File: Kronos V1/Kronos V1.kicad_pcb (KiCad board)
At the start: 4 copper layers, 65.6 x 91.8 mm, 229 parts, among them IC1 AS5600-ASOT, J1 USB_C_Receptacle_USB2.0_16P, Q1 BSS138, Q2 BSS138, U1 DM-OLED096-636, U10 ADS1115IDGS, U11 ADS1115IDGS, U12 WS2812-2020, U13 WS2812-2020, U14 WS2812-2020, U15 WS2812-2020, U16 WS2812-2020, U17 WS2812-2020, U18 WS2812-2020, U19 WS2812-2020, U2 ESP32-S3-MINI-1, U20 WS2812-2020, U21 WS2812-2020, U22 WS2812-2020, U23 WS2812-2020, U24 WS2812-2020, U25 WS2812-2020, U26 WS2812-2020, U27 WS2812-2020, U28 WS2812-2020, U29 WS2812-2020, U3 AMS1117-3.3, U30 WS2812-2020, U31 WS2812-2020, U32 WS2812-2020, U33 WS2812-2020, U34 WS2812-2020, U35 WS2812-2020, U36 WS2812-2020, U37 WS2812-2020, U38 WS2812-2020, U39 WS2812-2020, U4 AH49ENTR-G1, U40 WS2812-2020, U41 WS2812-2020, U42 WS2812-2020, U43 WS2812-2020, U44 WS2812-2020, U45 WS2812-2020, U46 WS2812-2020, U47 WS2812-2020, U48 WS2812-2020, U49 WS2812-2020, U5 AH49ENTR-G1, U50 WS2812-2020, U51 WS2812-2020, U52 WS2812-2020, U53 WS2812-2020, U54 WS2812-2020, U55 WS2812-2020, U56 WS2812-2020, U57 WS2812-2020, U58 WS2812-2020, U59 WS2812-2020, U6 AH49ENTR-G1, U60 WS2812-2020, U61 WS2812-2020, U62 WS2812-2020, U63 WS2812-2020, U64 WS2812-2020, U65 WS2812-2020, U66 WS2812-2020, U67 WS2812-2020, U68 WS2812-2020, U69 WS2812-2020, U7 AH49ENTR-G1, U70 WS2812-2020, U71 WS2812-2020, U72 WS2812-2020, U73 WS2812-2020, U74 WS2812-2020, U75 WS2812-2020, U76 WS2812-2020, U77 WS2812-2020, U78 WS2812-2020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

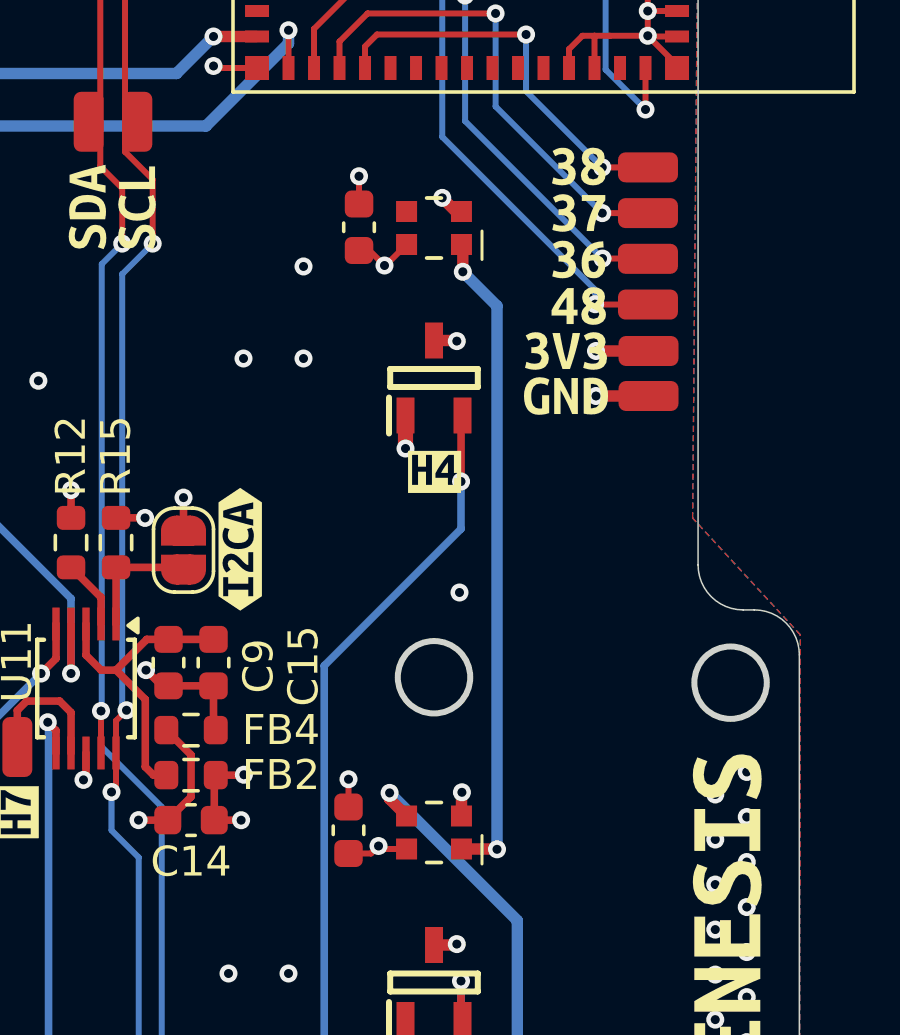
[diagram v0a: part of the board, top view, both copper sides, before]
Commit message: Corrected error with H4 ARGB
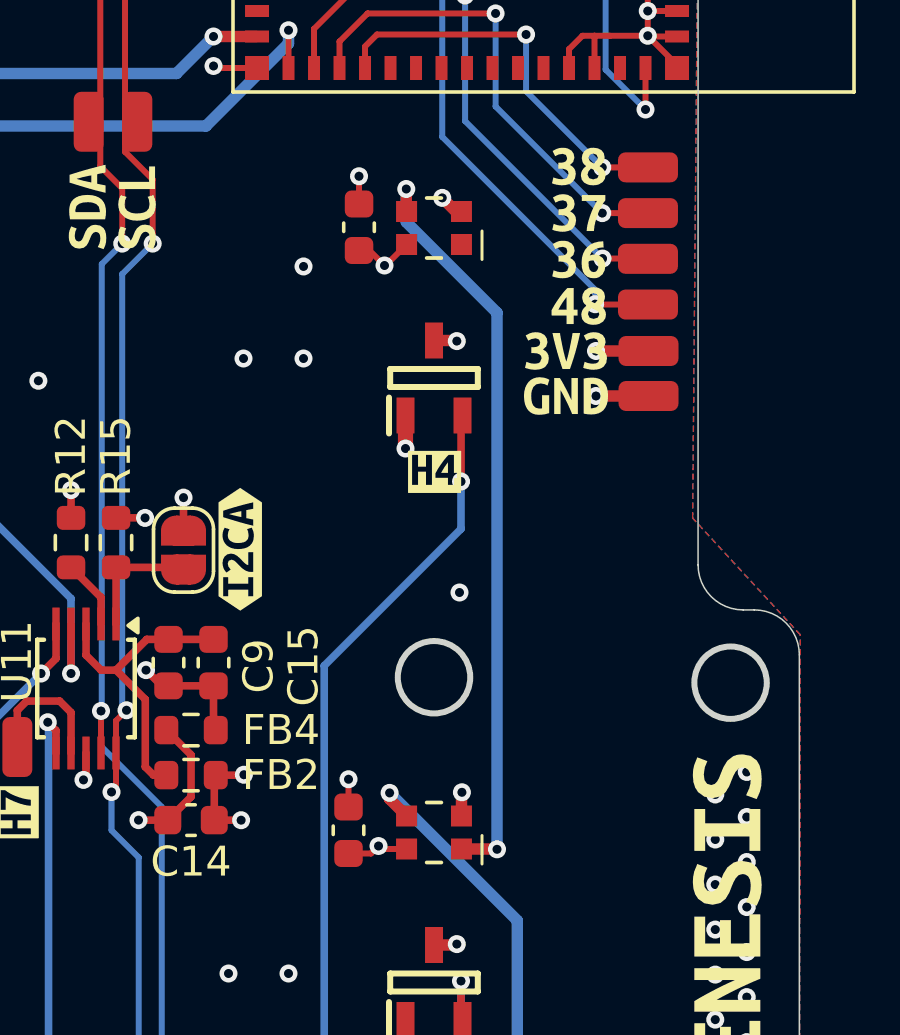
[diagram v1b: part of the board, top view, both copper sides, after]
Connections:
- U92 pad 1: Net-(U91-DO) -> unconnected-(U92-DO-Pad1)
- U92 pad 3: unconnected-(U92-DI-Pad3) -> Net-(U91-DO)
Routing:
- net Net-(U91-DO): track 21.8 -> 25.2 mm
